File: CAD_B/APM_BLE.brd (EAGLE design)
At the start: 26.7 x 47.2 mm, 33 parts, among them J1 CON_HEADER_PRG_AVR_ICSP-PTH, J2 B2B-PH-K-S(LF)(SN), Q1 8MHz, Q2 PMV48XP, Q3 PMV48XP, U1 ATMEGA328P, U3 JDY-08

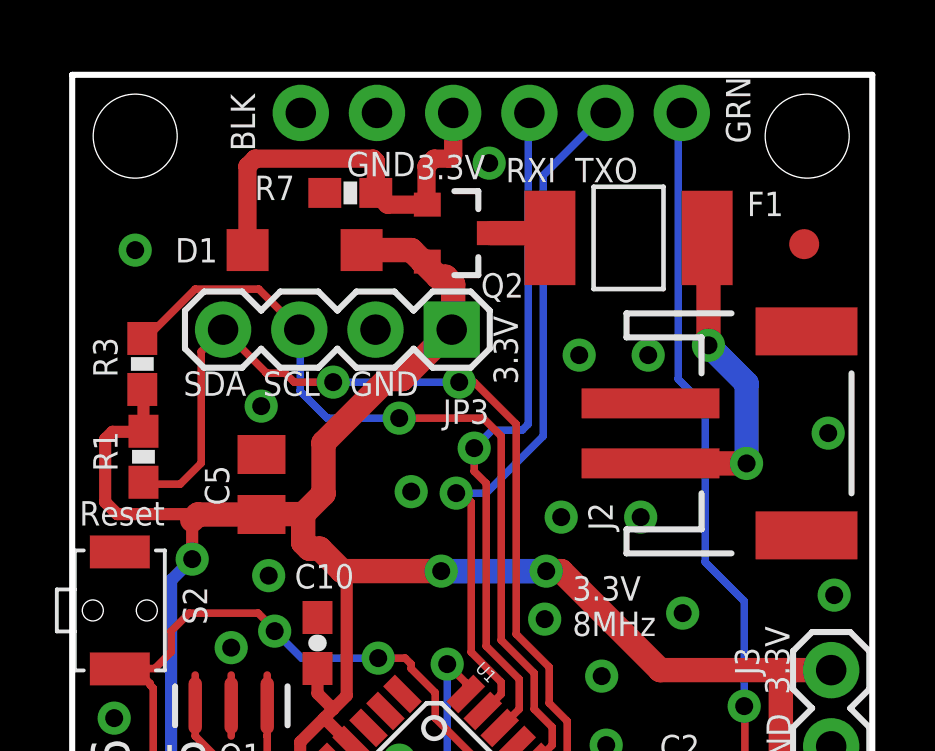
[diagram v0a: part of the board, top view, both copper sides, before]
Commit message: pnums added and cap change
Changed 10uF cap to 0603, updated PCB
added farnell pnums
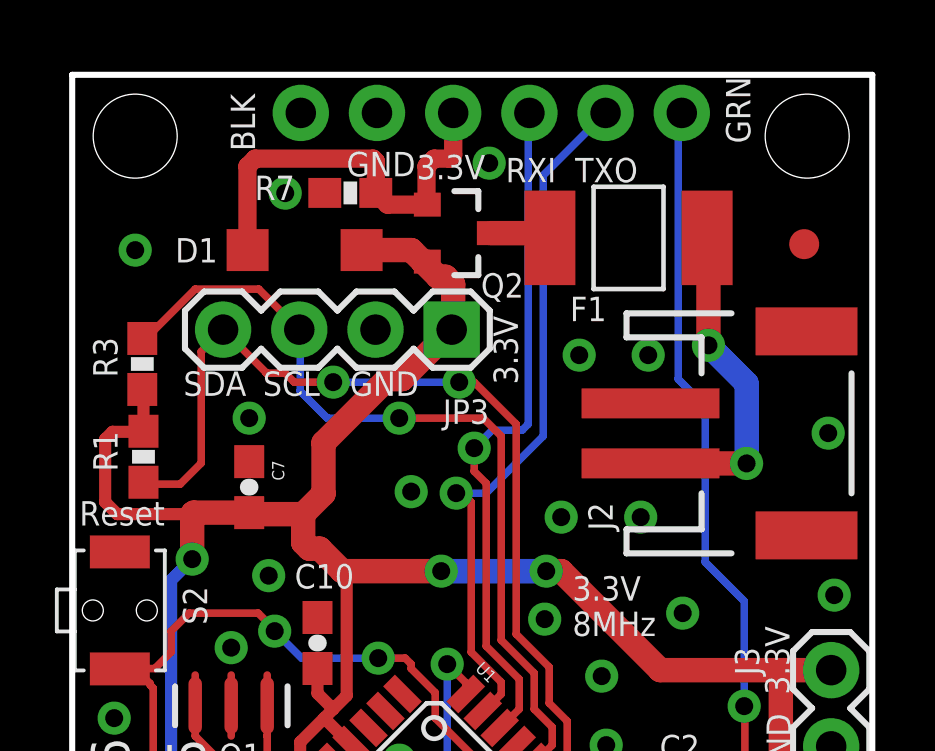
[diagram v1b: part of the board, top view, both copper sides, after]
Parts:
- removed C5: 10uF, rcl:C0805K
- added C7: 10uF, SparkFun:0603-CAP
- J2: value B2B-PH-K-S(LF)(SN) -> S2B-PH-SM4-TB(LF)(SN)
- J3, JP3: value (none) -> 1X4 PIN HEADER
- J4, JP2: value (none) -> NO_FIT
- Q1: value 8MHz -> 8MHz CSTCE8M00G55-R0
- Q2, Q3: value PMV48XP -> PMV48XP or DMP2035U
- R2: value 10K -> 10K, 1%
- R4: value 200k 1% -> 200k, 1%
- R5: value 100k 1% -> 100k, 1%
- R7: value 100k -> 100k, 1%
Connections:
- net N$4 renamed FS_D
- net +3V3: now also C7.2; no longer C5.1
- net GND: now also C7.1; no longer C5.2
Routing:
- net GND: vias 40 -> 41

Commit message: Minor updates
Minor Updates
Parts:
- added C11, C9: 22pF, SparkFun:0603-CAP
- added C5: 0.1uF, SparkFun:0603-CAP
- added C8: 10uF, SparkFun:0603-CAP
- added Q4: 8MHz, adafruit:HC49UP
- added Q5: (no value), crystal:CTS406
- added R8, R9: 0R0, SparkFun:0603-RES
- added S1: MOMENTARY-SWITCH-SPST-SMD-6.0X3.5MM, SparkFun-Switches:TACTILE_SWITCH_SMD_6.0X3.5MM
- added U2: TSYS01, TSYS01:QFN65P400X400X90-17N
- F1: value MF-MSMF050-2 500mA -> MSMF110-2, 1.1A
- Q1: value 8MHz CSTCE8M00G55-R0 -> 8MHz CSTCE8M00G55-R0
- R4: value 200k, 1% -> 390k, 1%
- moved S2 17.7 mm to (19.2, 28.1), turned to 0 degrees
- moved R3 0.30 mm to (2.34, 37.9)
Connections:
- removed net A4: JP3.4, R1.1, U1.27
- removed net A5: JP3.3, R3.1, U1.28
- new net A4_SDA: JP3.4, R1.1, U1.27, U2.4
- new net A5_SCL: JP3.3, R3.1, U1.28, U2.3
- new net N$10: R8.1, U2.16
- new net N$4: R9.1, U2.2
- new net N$6: U2.10, U2.11
- net +3V3: now also C5.2, C8.2, R8.2, R9.2, U2.15
- net BLE_CONSTAT: now also U3.6; no longer U3.P16/CONSTATN
- net BLE_DC: now also U3.2; no longer U3.P22/DEBUGCLOCK
- net BLE_DD: now also U3.3; no longer U3.P21/DEBUGDATA
- net BLE_IO1: now also U3.8; no longer U3.P12/IO1
- net BLE_PWM1: now also U3.14; no longer U3.P10/PWM1
- net D2: now also U3.19; no longer U3.P03/TXDOUT
- net D5: now also U3.22; no longer U3.P00/PWRCN
- net D6: now also U3.23; no longer U3.RSTIN
- net D9: now also U3.20; no longer U3.P02/RXDIN
- net GND: now also C5.1, C8.1, U2.1, U2.17, U3.24; no longer U3.GND
- net V+: now also U3.1; no longer U3.VCC_3.3
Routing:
- net A4: track 30.8 -> 0.00 mm, vias 2 -> 0
- net A4_SDA: track 0.00 -> 30.7 mm, vias 0 -> 2
- net A5_SCL: track 0.00 -> 28.3 mm, vias 0 -> 1
- net A5: track 27.8 -> 0.00 mm, vias 1 -> 0
- net RESET: track 31.8 -> 36.2 mm
- net +3V3: track 103.5 -> 106.8 mm, vias 7 -> 5
